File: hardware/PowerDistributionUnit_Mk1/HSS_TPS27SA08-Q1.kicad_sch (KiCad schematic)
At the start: 29 parts, among them U3 TPS27SA08CQPWPRQ1, U32 ACS37042KLHBLT-010B3

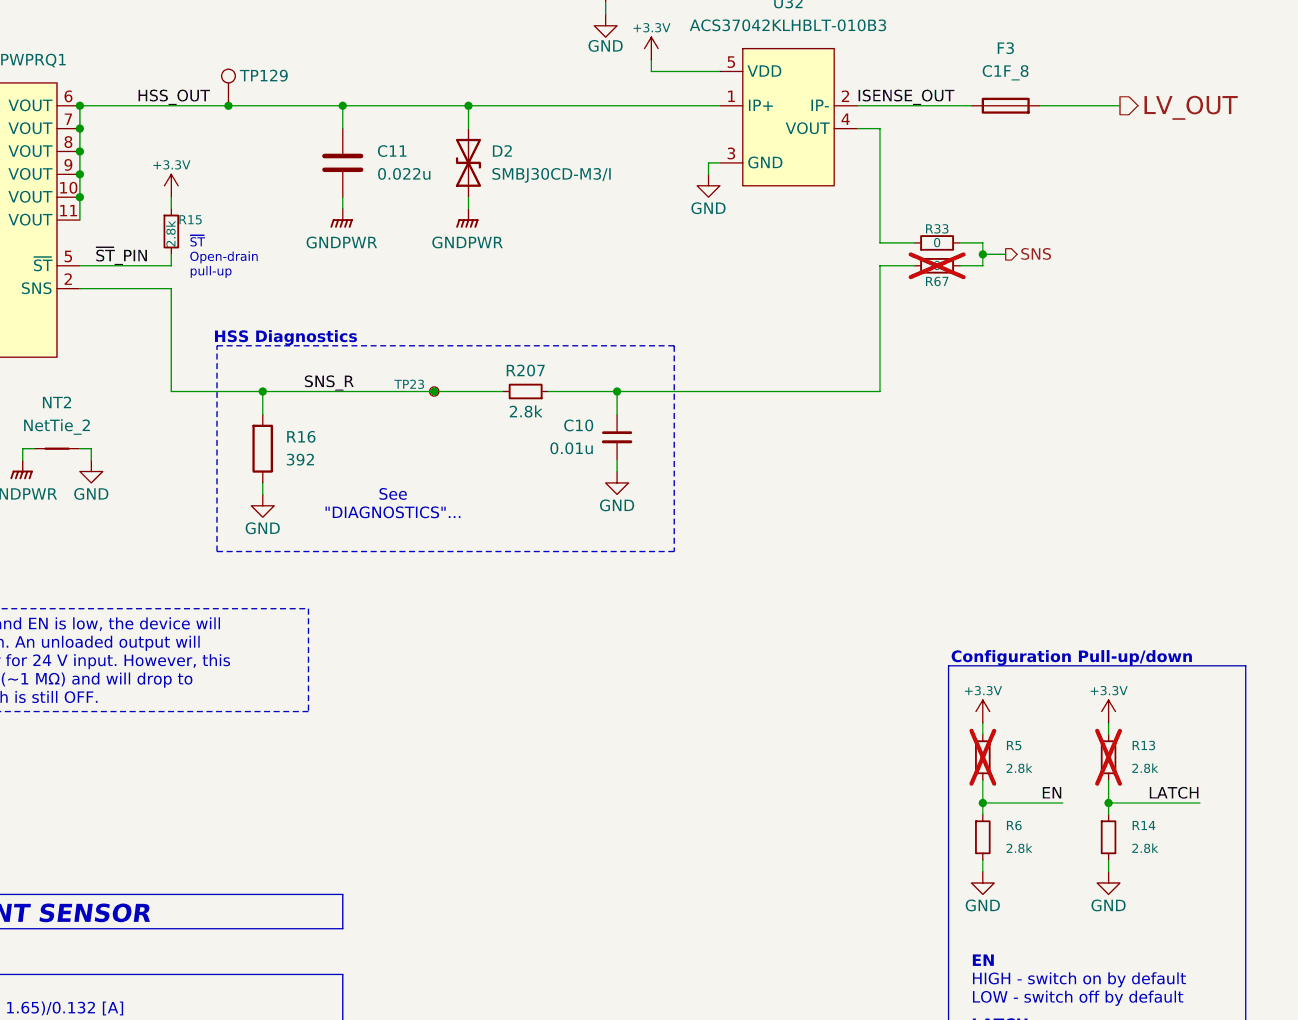
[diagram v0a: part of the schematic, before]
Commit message: change lv sense rdiv values to avoid extended components, update all pull-ups/-downs using 2.8k
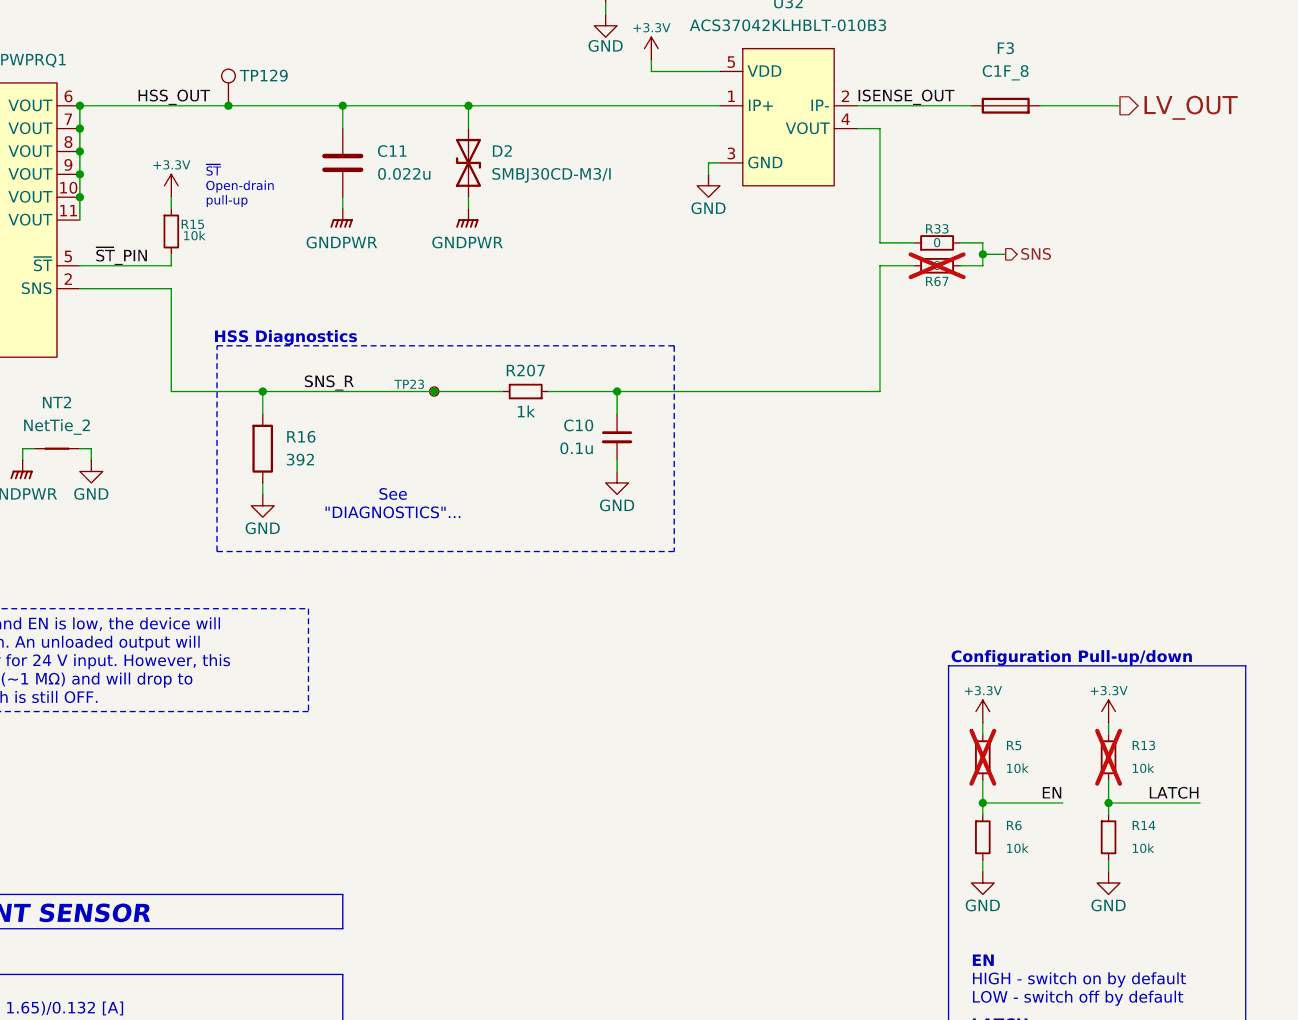
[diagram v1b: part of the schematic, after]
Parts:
- C10: value 0.01u -> 0.1u; symbol PowerDistributionUnitCapacitorLib:0.01u_Small -> PowerDistributionUnitCapacitorLib:0.1u_Small; LCSC P/N C57112 -> C14663; Mouser P/N 963-MSASH168SB5103KT -> 963-MLASH168SB7104KT; P/N MSASH168SB5103KTNA01 -> MLASH168SB7104KTNA01
- R13, R14, R15, R5, R6: value 2.8k -> 10k; symbol PowerDistributionUnitResistorLib:2.8k_Small -> PowerDistributionUnitResistorLib:10k_Small; LCSC P/N C844548 -> C25804; Mouser P/N 71-CRCW0603-2.8K-E3 -> 71-CRCW060310K0FKEI; P/N CRCW06032K80FKEA -> CRCW060310K0FKEI
- R207: value 2.8k -> 1k; symbol PowerDistributionUnitResistorLib:2.8k_Small -> PowerDistributionUnitResistorLib:1k_Small; Digikey P/N 541-2.80KHCT-ND -> 541-CRCW06031K00FKEECT-ND; LCSC P/N C844548 -> C21190; Mouser P/N 71-CRCW0603-2.8K-E3 -> 71-CRCW06031K00FKEI; P/N CRCW06032K80FKEA -> CRCW06031K00FKEI
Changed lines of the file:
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@@
 	(text "~{ST}\nOpen-drain\npull-up"
 		(exclude_from_sim no)
-		(at 155.702 62.738 0)
+		(at 157.48 54.864 0)
 		(effects
 			(font
@@
 	)
 	(symbol
-		(lib_id "PowerDistributionUnitResistorLib:2.8k_Small")
+		(lib_id "PowerDistributionUnitResistorLib:10k_Small")
 		(at 257.81 127 0)
 		(unit 1)
@@
 			)
 		)
-		(property "Value" "2.8k"
+		(property "Value" "10k"
 			(at 260.35 128.27 0)
 			(effects
@@
 			)
 		)
-		(property "P/N" "CRCW06032K80FKEA"
+		(property "P/N" "CRCW060310K0FKEI"
 			(at 257.81 127 0)
 			(effects
@@
 			)
 		)
-		(property "Mouser P/N" "71-CRCW0603-2.8K-E3"
+		(property "Mouser P/N" "71-CRCW060310K0FKEI"
 			(at 257.81 127 0)
 			(effects
@@
 			)
 		)
-		(property "LCSC P/N" "C844548"
+		(property "LCSC P/N" "C25804"
 			(at 257.81 127 0)
 			(effects
@@
 	)
 	(symbol
-		(lib_id "PowerDistributionUnitResistorLib:2.8k_Small")
+		(lib_id "PowerDistributionUnitResistorLib:10k_Small")
 		(at 243.84 118.11 0)
 		(unit 1)
@@
 			)
 		)
-		(property "Value" "2.8k"
+		(property "Value" "10k"
 			(at 246.38 119.38 0)
 			(effects
@@
 			)
 		)
-		(property "P/N" "CRCW06032K80FKEA"
+		(property "P/N" "CRCW060310K0FKEI"
 			(at 243.84 118.11 0)
 			(effects
@@
 			)
 		)
-		(property "Mouser P/N" "71-CRCW0603-2.8K-E3"
+		(property "Mouser P/N" "71-CRCW060310K0FKEI"
 			(at 243.84 118.11 0)
 			(effects
@@
 			)
 		)
-		(property "LCSC P/N" "C844548"
+		(property "LCSC P/N" "C25804"
 			(at 243.84 118.11 0)
 			(effects
@@
 	)
 	(symbol
-		(lib_id "PowerDistributionUnitResistorLib:2.8k_Small")
+		(lib_id "PowerDistributionUnitResistorLib:10k_Small")
 		(at 257.81 118.11 0)
 		(unit 1)
@@
 			)
 		)
-		(property "Value" "2.8k"
+		(property "Value" "10k"
 			(at 260.35 119.38 0)
 			(effects
@@
 			)
 		)
-		(property "P/N" "CRCW06032K80FKEA"
+		(property "P/N" "CRCW060310K0FKEI"
 			(at 257.81 118.11 0)
 			(effects
@@
 			)
 		)
-		(property "Mouser P/N" "71-CRCW0603-2.8K-E3"
+		(property "Mouser P/N" "71-CRCW060310K0FKEI"
 			(at 257.81 118.11 0)
 			(effects
@@
 			)
 		)
-		(property "LCSC P/N" "C844548"
+		(property "LCSC P/N" "C25804"
 			(at 257.81 118.11 0)
 			(effects
@@
 	)
 	(symbol
-		(lib_id "PowerDistributionUnitResistorLib:2.8k_Small")
+		(lib_id "PowerDistributionUnitResistorLib:10k_Small")
 		(at 243.84 127 0)
 		(unit 1)
@@
 			)
 		)
-		(property "Value" "2.8k"
+		(property "Value" "10k"
 			(at 246.38 128.27 0)
 			(effects
@@
 			)
 		)
-		(property "P/N" "CRCW06032K80FKEA"
+		(property "P/N" "CRCW060310K0FKEI"
 			(at 243.84 127 0)
 			(effects
@@
 			)
 		)
-		(property "Mouser P/N" "71-CRCW0603-2.8K-E3"
+		(property "Mouser P/N" "71-CRCW060310K0FKEI"
 			(at 243.84 127 0)
 			(effects
@@
 			)
 		)
-		(property "LCSC P/N" "C844548"
+		(property "LCSC P/N" "C25804"
 			(at 243.84 127 0)
 			(effects
@@
 	)
 	(symbol
-		(lib_id "PowerDistributionUnitCapacitorLib:0.01u_Small")
+		(lib_id "PowerDistributionUnitCapacitorLib:0.1u_Small")
 		(at 203.2 82.55 0)
 		(mirror y)
@@
 			)
 		)
-		(property "Value" "0.01u"
+		(property "Value" "0.1u"
 			(at 200.66 83.8262 0)
 			(effects
@@
 			)
 		)
-		(property "Datasheet" "kicad-embed://Tayio_Yuden_1102023_MS_mlcc_all_e.pdf"
+		(property "Datasheet" "kicad-embed://MSR01_e.pdf"
 			(at 203.2 82.55 0)
 			(effects
@@
 			)
 		)
-		(property "P/N" "MSASH168SB5103KTNA01"
+		(property "P/N" "MLASH168SB7104KTNA01"
 			(at 203.2 82.55 0)
 			(effects
@@
 			)
 		)
-		(property "Mouser P/N" "963-MSASH168SB5103KT"
+		(property "Mouser P/N" "963-MLASH168SB7104KT"
 			(at 203.2 82.55 0)
 			(effects
@@
 			)
 		)
-		(property "LCSC P/N" "C57112"
+		(property "LCSC P/N" "C14663"
 			(at 203.2 82.55 0)
 			(effects
@@
 	)
 	(symbol
-		(lib_id "PowerDistributionUnitResistorLib:2.8k_Small")
+		(lib_id "PowerDistributionUnitResistorLib:1k_Small")
 		(at 193.04 77.47 270)
 		(mirror x)
@@
 			)
 		)
-		(property "Value" "2.8k"
+		(property "Value" "1k"
 			(at 193.04 79.756 90)
 			(effects
@@
 			)
 		)
-		(property "P/N" "CRCW06032K80FKEA"
+		(property "P/N" "CRCW06031K00FKEI "
 			(at 193.04 77.47 0)
 			(effects
@@
 			)
 		)
-		(property "Mouser P/N" "71-CRCW0603-2.8K-E3"
+		(property "Mouser P/N" "71-CRCW06031K00FKEI"
 			(at 193.04 77.47 0)
 			(effects
@@
 			)
 		)
-		(property "Digikey P/N" "541-2.80KHCT-ND"
+		(property "Digikey P/N" "541-CRCW06031K00FKEECT-ND"
 			(at 193.04 77.47 0)
 			(effects
@@
 			)
 		)
-		(property "LCSC P/N" "C844548"
+		(property "LCSC P/N" "C21190"
 			(at 193.04 77.47 0)
 			(effects
@@
 	)
 	(symbol
-		(lib_id "PowerDistributionUnitResistorLib:2.8k_Small")
+		(lib_id "PowerDistributionUnitResistorLib:10k_Small")
 		(at 153.67 59.69 0)
 		(unit 1)
@@
 		(dnp no)
 		(property "Reference" "R15"
-			(at 154.432 58.42 0)
+			(at 154.686 58.928 0)
 			(effects
 				(font
@@
 			)
 		)
-		(property "Value" "2.8k"
-			(at 153.67 61.468 90)
+		(property "Value" "10k"
+			(at 156.21 60.198 0)
 			(effects
 				(font
 					(size 1 1)
 				)
-				(justify left)
 			)
 		)
@@
 			)
 		)
-		(property "P/N" "CRCW06032K80FKEA"
+		(property "P/N" "CRCW060310K0FKEI"
 			(at 153.67 59.69 0)
 			(effects
@@
 			)
 		)
-		(property "Mouser P/N" "71-CRCW0603-2.8K-E3"
+		(property "Mouser P/N" "71-CRCW060310K0FKEI"
 			(at 153.67 59.69 0)
 			(effects
@@
 			)
 		)
-		(property "LCSC P/N" "C844548"
+		(property "LCSC P/N" "C25804"
 			(at 153.67 59.69 0)
 			(effects
